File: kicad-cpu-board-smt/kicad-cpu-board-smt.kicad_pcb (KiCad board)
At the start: 2 copper layers, 78.5 x 69 mm, 56 parts, among them J1 ICSP Header, J2 Conn_01x10_Male, J3 Conn_01x16_Female, J4 Conn_02x05_Odd_Even, Q1 2N7002, Q2 2N7002, Q3 2N7002, Q4 2N7002, U1 AMS1117-5.0, U2 AMS1117-3.3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

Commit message: Updating CPU board silkscreen
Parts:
- added REF***: OSHW-Logo2_7.3x6mm_Copper, Symbols:OSHW-Logo2_7.3x6mm_Copper, F.Cu at (57.9, 25.4)
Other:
- board text added: "SUPER SIXTEEN V1.4 SMT"
- board text removed: "."
- board text removed: "SUPER SIXTEEN V1.3 SMT"

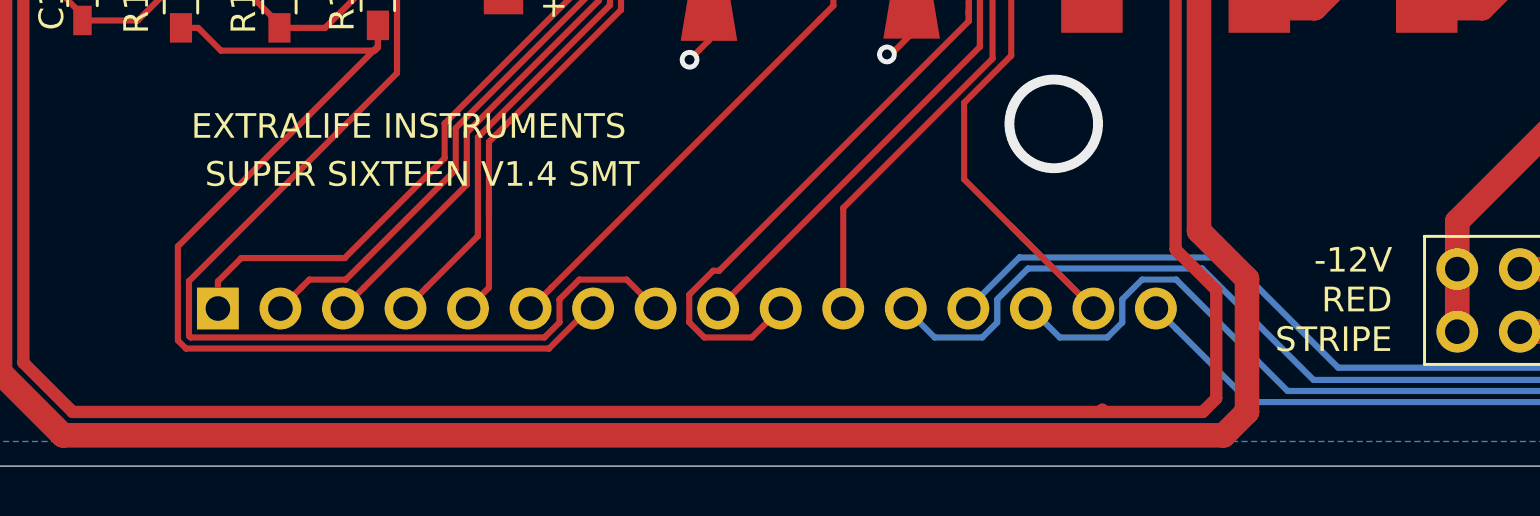
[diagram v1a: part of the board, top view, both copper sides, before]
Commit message: Updating silkscreen on SMT cpu board
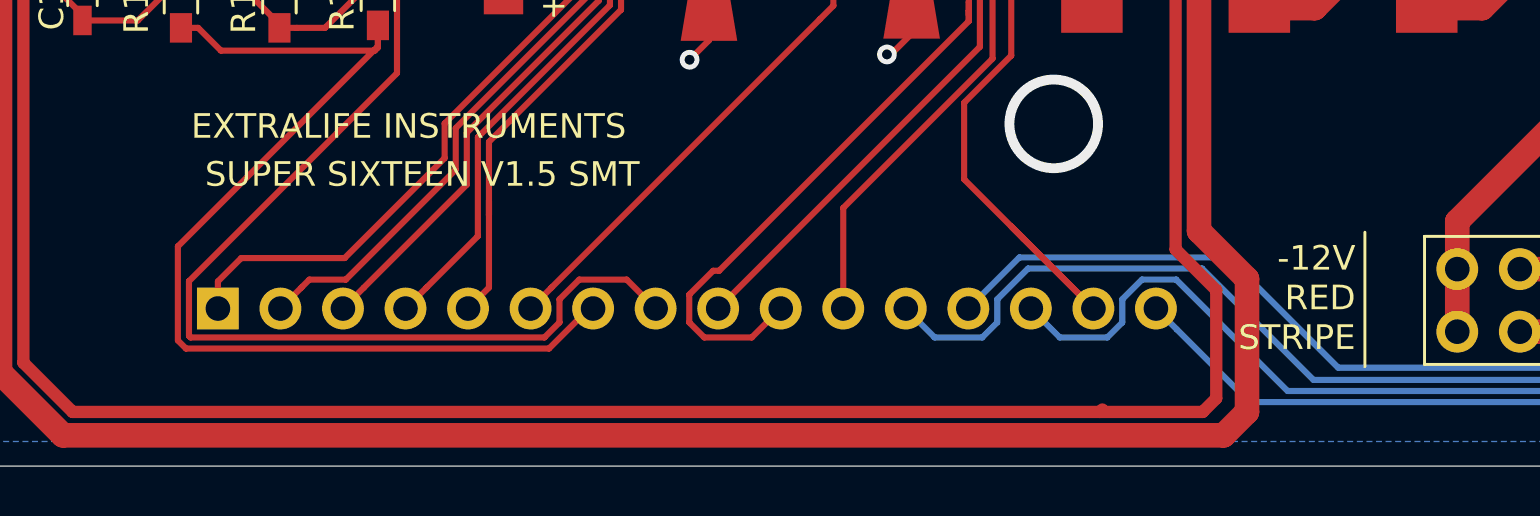
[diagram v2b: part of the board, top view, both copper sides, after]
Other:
- board text added: "SUPER SIXTEEN V1.5 SMT"
- board text removed: "SUPER SIXTEEN V1.4 SMT"
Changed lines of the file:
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@@
   (general
     (thickness 1.6)
-    (drawings 52)
+    (drawings 53)
     (tracks 968)
     (zones 0)
@@
     )
   )
+  (gr_line (start 69.088 71.501) (end 69.088 76.962) (layer F.SilkS) (width 0.12))
   (gr_line (start 86.614 58.928) (end 88.519 58.928) (layer F.SilkS) (width 0.12))
   (gr_line (start 82.804 58.928) (end 84.582 58.928) (layer F.SilkS) (width 0.12))
@@
     (effects (font (size 1 1) (thickness 0.15)))
   )
-  (gr_text "-12V\nRED\nSTRIPE" (at 70.2 74.25) (layer F.SilkS)
+  (gr_text "-12V\nRED\nSTRIPE" (at 68.707 74.168) (layer F.SilkS)
     (effects (font (size 1 1) (thickness 0.15)) (justify right))
   )
-  (gr_text "SUPER SIXTEEN V1.4 SMT" (at 30.8 69.15) (layer F.SilkS)
+  (gr_text "SUPER SIXTEEN V1.5 SMT" (at 30.8 69.15) (layer F.SilkS)
     (effects (font (size 1 1) (thickness 0.15)))
   )
